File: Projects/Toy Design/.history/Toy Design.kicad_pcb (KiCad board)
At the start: 2 copper layers, 170 x 120 mm, 85 parts, among them J1 Conn_01x01_Pin, J2 Conn_01x01_Pin, J3 FTSH-107-01-X-DV-K-TR, SW1 5GTH935, SW2 5GTH935, U1 TLV61048DBVR, U10 STM32G030K6T6, U11 MCP3208-CI/SL, U12 74HC595, U13 74HC595, U14 74HC595, U15 74HC595, U16 74HC595, U17 74HC595, U2 MCP73123, U3 NCP1117-5.0_SOT223, U4 MLX90333, U5 A1330, U6 A1330, U7 NCP1117-3.3_SOT223, U8 A1330, U9 TXU0104

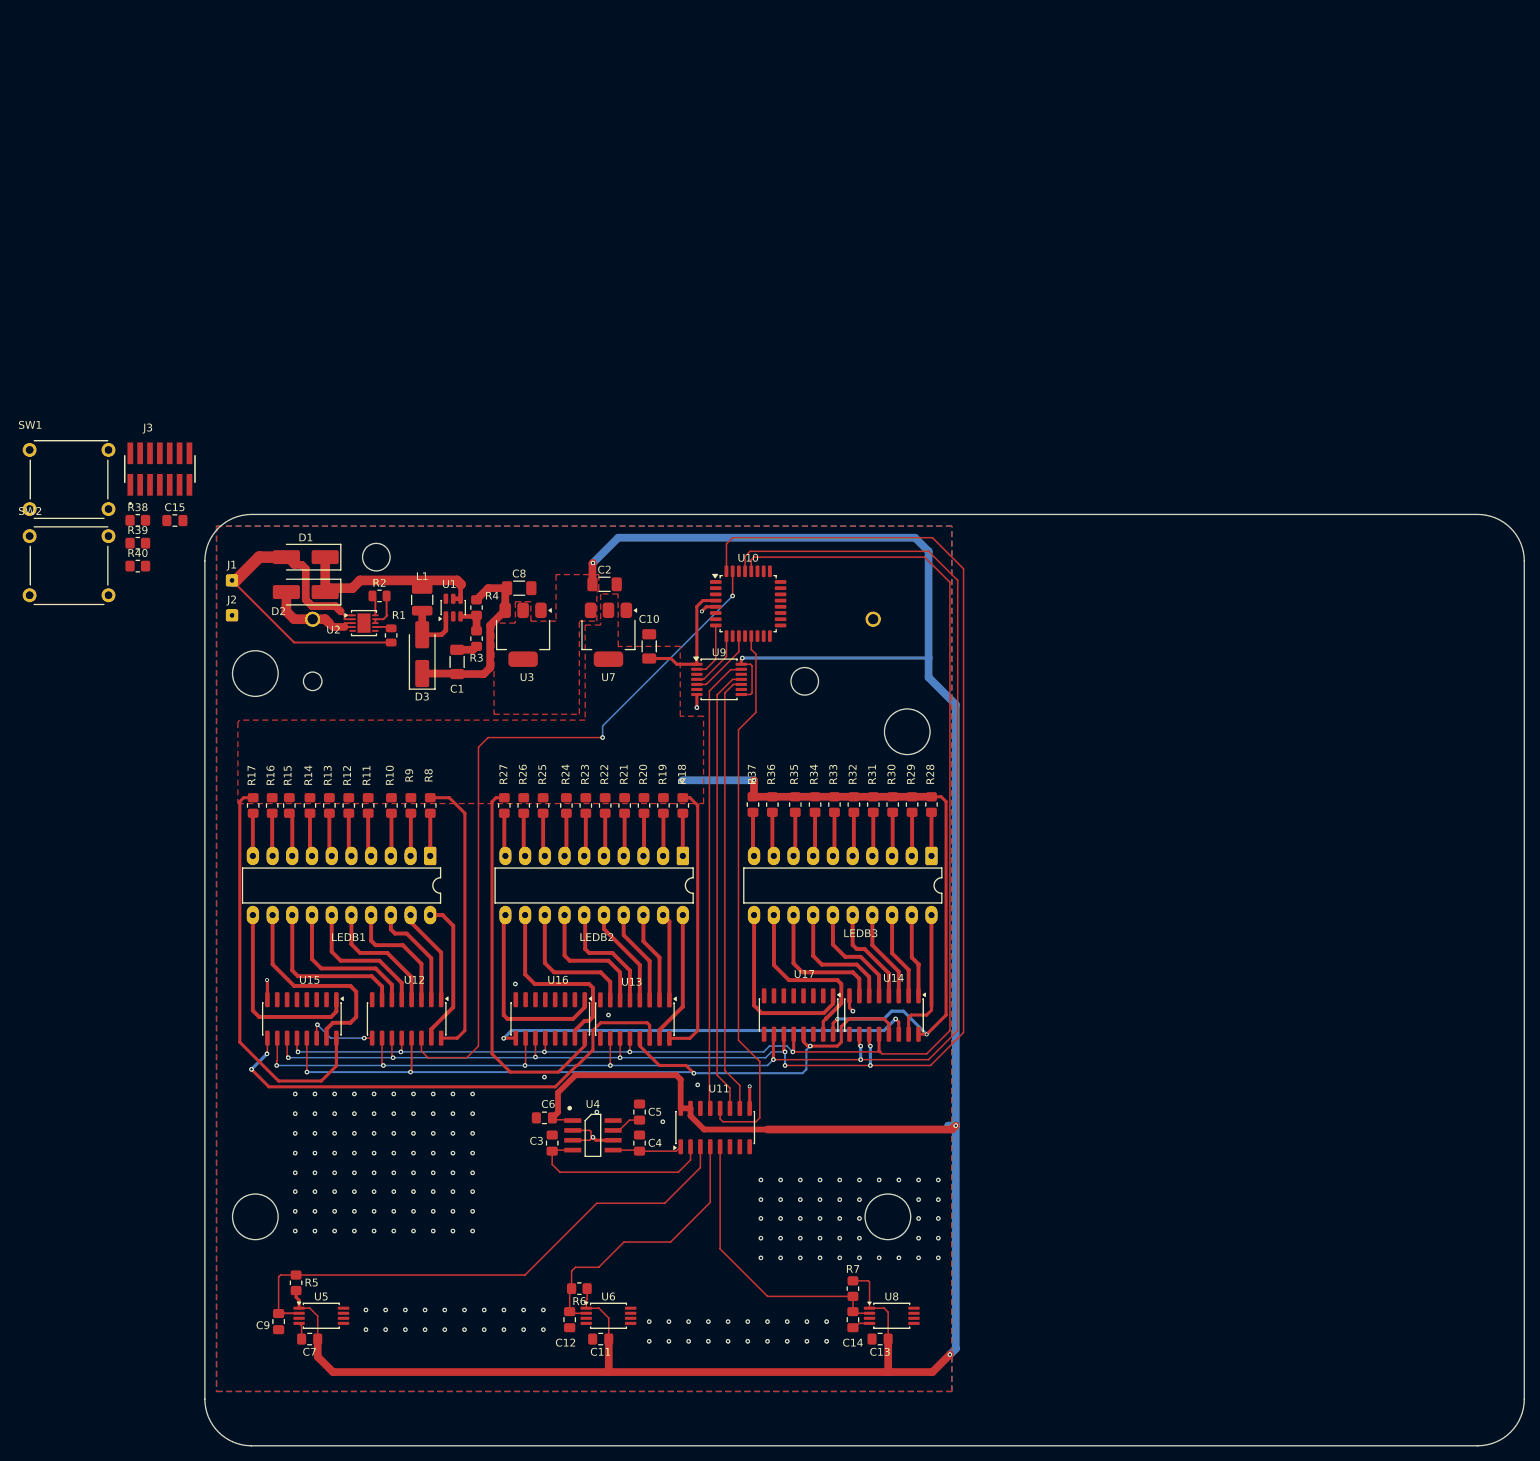
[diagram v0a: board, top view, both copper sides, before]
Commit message: Continued layout on design file with claude
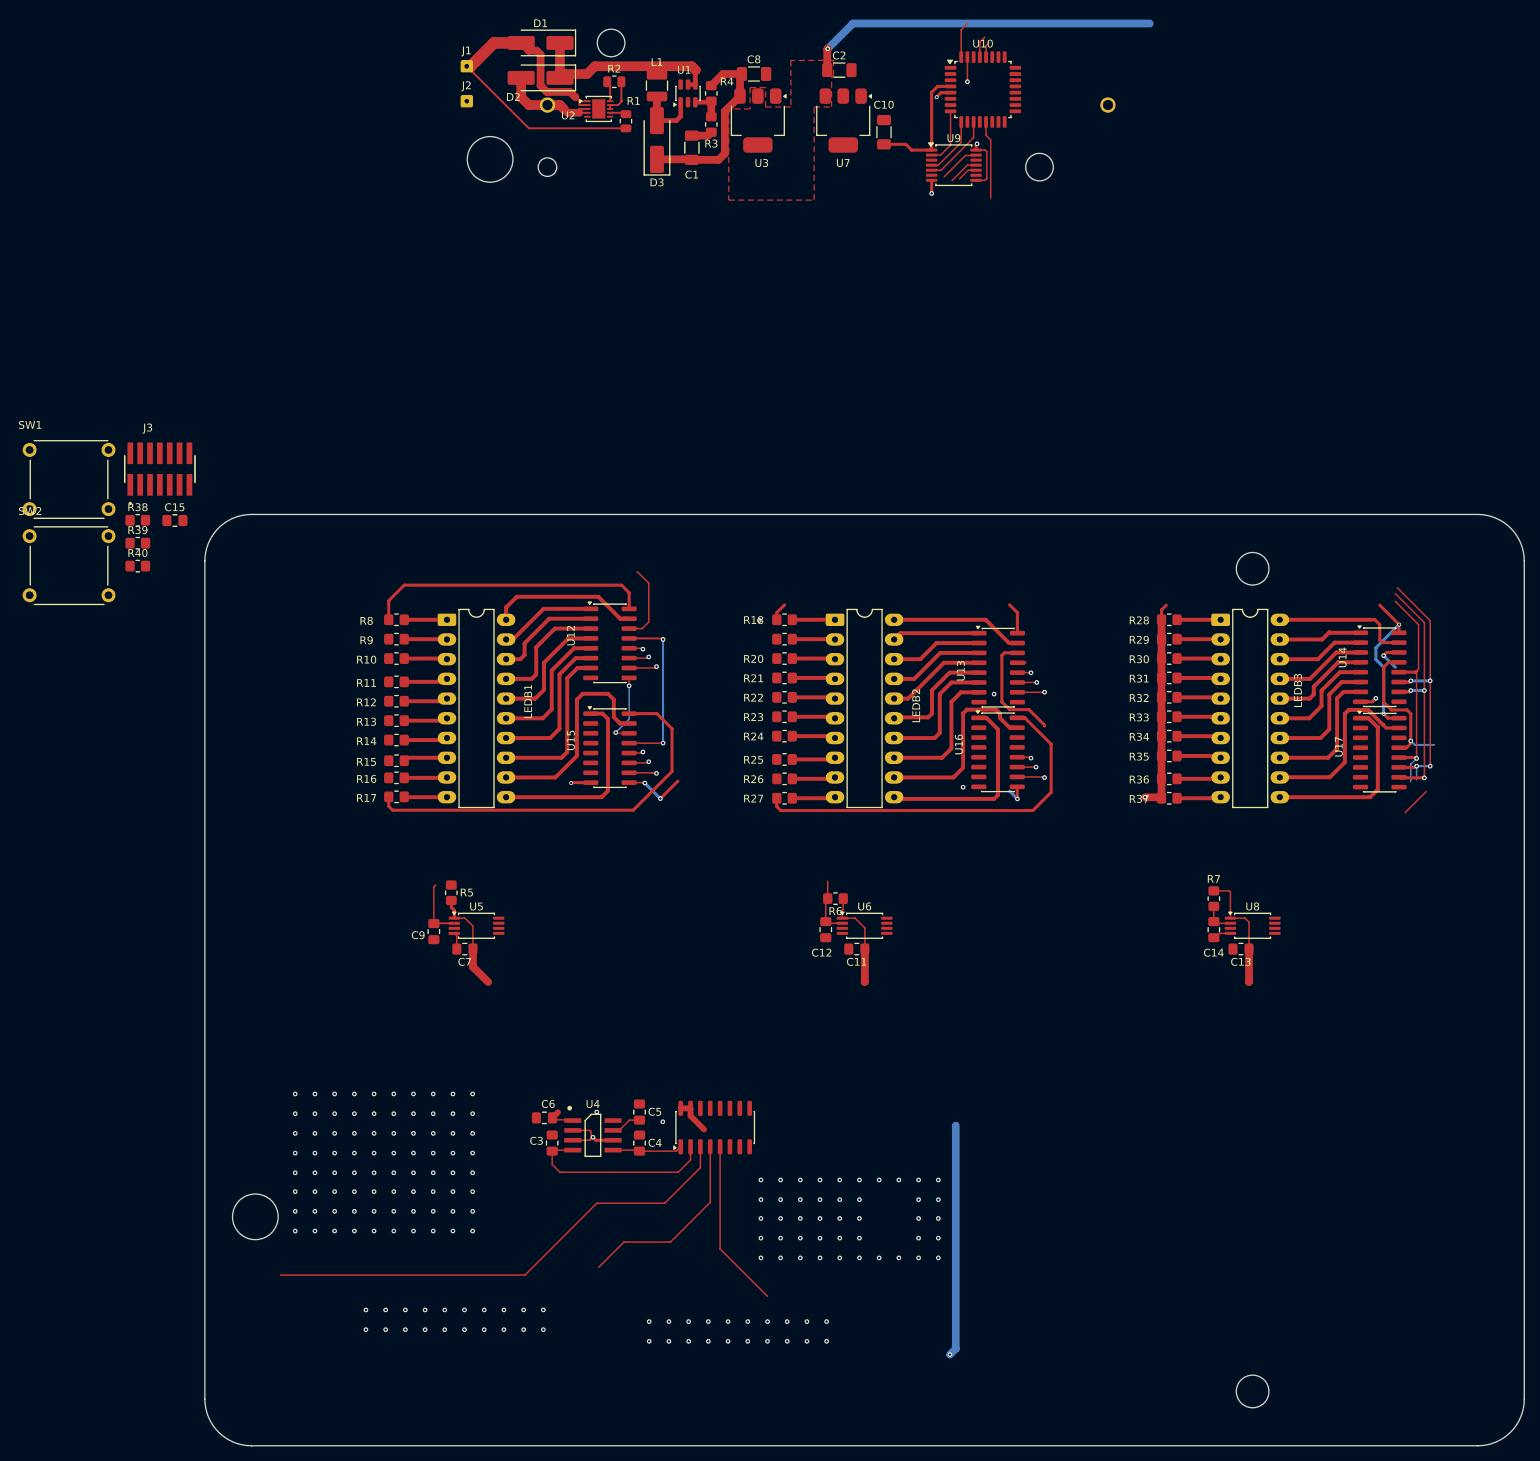
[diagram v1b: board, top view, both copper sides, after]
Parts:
- moved U17 82.2 mm to (247.9, 62.2), turned to 0 degrees
- moved U14 78.0 mm to (247.9, 51.2), turned to 0 degrees
- moved BT1 72.8 mm to (176.8, -21.2)
- moved C1 72.8 mm to (159.2, -15.8)
- moved C10 72.8 mm to (184.0, -17.8)
- moved C2 72.8 mm to (178.2, -25.8)
- moved C8 72.8 mm to (167.2, -25.2)
- moved D1 72.8 mm to (139.8, -29.2)
- moved D2 72.8 mm to (139.8, -24.8)
- moved D3 72.8 mm to (154.8, -16.8)
- moved J1 72.8 mm to (130.2, -26.2)
- moved J2 72.8 mm to (130.2, -21.8)
- moved L1 72.8 mm to (154.8, -23.8)
- moved R1 72.8 mm to (150.8, -19.2)
- moved R2 72.8 mm to (149.2, -24.2)
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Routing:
- net +5V: track 372.7 -> 133.5 mm, vias 4 -> 3
- net SPI2_SCK_LED: track 203.3 -> 49.6 mm
- net ~{SRCLR}: track 199.6 -> 49.0 mm
- net RCLK_LED: track 184.2 -> 38.8 mm
- net SPI2_MOSI_LED: track 93.4 -> 13.2 mm, vias 2 -> 1
- net +3.3V: track 274.3 -> 208.5 mm
- net ~{OE}: track 102.6 -> 42.9 mm, vias 4 -> 3
- net MISO_SPI1: track 71.2 -> 14.0 mm
- net Net-(U11-~{CS}/SHDN): track 56.9 -> 2.57 mm
- net Net-(U11-Din): track 57.9 -> 3.94 mm
- net Net-(U11-CLK): track 59.1 -> 5.27 mm
- net Net-(U14-SER): track 55.2 -> 7.24 mm
- net Net-(U13-SER): track 63.8 -> 23.0 mm
- net OUT_U8: track 37.0 -> 26.0 mm
- net OUT_U6: track 36.2 -> 32.5 mm
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- removed copper zone on F.Cu, net +3.3V
- removed copper zone on B.Cu, net GND
- removed copper zone on F.Cu, net GND
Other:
- board size 170 x 120 mm -> 170 x 168.7 mm

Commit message: final update from desktop
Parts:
- moved SW2 204.6 mm to (255.5, 141.5)
- moved BT1 126.9 mm to (146.5, 102.0)
- moved C1 126.9 mm to (129.0, 107.5)
- moved C10 126.9 mm to (153.8, 105.5)
- moved C2 126.9 mm to (148.0, 97.5)
- moved C8 126.9 mm to (137.0, 98.0)
- moved D1 126.9 mm to (109.5, 94.0)
- moved D2 126.9 mm to (109.5, 98.5)
- moved D3 126.9 mm to (124.5, 106.5)
- moved J1 126.9 mm to (100.0, 97.0)
- moved J2 126.9 mm to (100.0, 101.5)
- moved L1 126.9 mm to (124.5, 99.5)
- moved R1 126.9 mm to (120.5, 104.1)
- moved R2 126.9 mm to (119.0, 99.0)
- moved R3 126.9 mm to (131.5, 104.5)
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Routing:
- net OUT_U5: track 70.2 -> 10.4 mm
- net +5V: track 133.5 -> 103.6 mm, vias 3 -> 4
- net OUT_U6: track 32.5 -> 7.54 mm
- net OUT_U8: track 26.0 -> 4.19 mm
- net +3.3V: track 208.5 -> 210.5 mm
- net Net-(U12-QA): track 19.2 -> 17.7 mm
- net GND: vias 173 -> 171
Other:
- board size 170 x 168.7 mm -> 170 x 120 mm

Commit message: small updates
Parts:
- J3: moved to B.Cu
- moved R38 127.2 mm to (198.5, 95.0), turned to 180 degrees
- moved C15 124.3 mm to (198.5, 97.5)
- moved J3 123.6 mm to (191.2, 97.5), turned to 90 degrees
- moved R39 111.2 mm to (175.0, 104.2), turned to 180 degrees
- moved R40 107.5 mm to (170.2, 107.2), turned to 180 degrees
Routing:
- net +5V: track 103.6 -> 161.5 mm, vias 4 -> 6
- net Net-(U10-PB1): track 0.00 -> 4.73 mm
- net Net-(U10-PB0): track 0.00 -> 3.39 mm
- net NRST: track 0.00 -> 2.52 mm

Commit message: updates
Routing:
- net ~{OE}: track 42.9 -> 115.0 mm, vias 3 -> 4
- net SPI2_MOSI_LED: track 13.2 -> 48.4 mm
- net ~{SRCLR}: track 49.0 -> 62.8 mm
- net SPI2_SCK_LED: track 49.6 -> 63.1 mm
- net RCLK_LED: track 38.8 -> 52.0 mm
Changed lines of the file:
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@@
+	)
+	(segment
+		(start 152.94 62.11)
+		(end 152.94 48.86)
+		(width 0.2)
+		(layer "B.Cu")
+		(net "RCLK_LED")
 	)
 	(segment
@@
 	)
 	(segment
+		(start 154.69 51.11)
+		(end 154.69 64.86)
+		(width 0.2)
+		(layer "B.Cu")
+		(net "~{SRCLR}")
+	)
+	(segment
 		(start 251.88 54.19)
 		(end 253.63 54.19)
@@
 	)
 	(segment
-		(start 152.19 38.86)
-		(end 153.69 40.36)
+		(start 151.165 46.205)
+		(end 154.983529 46.205)
 		(width 0.2)
 		(layer "F.Cu")
@@
 	)
 	(segment
-		(start 153.69 45.36)
-		(end 152.845 46.205)
-		(width 0.2)
-		(layer "F.Cu")
-		(net "SPI2_MOSI_LED")
-	)
-	(segment
-		(start 152.845 46.205)
-		(end 151.165 46.205)
-		(width 0.2)
-		(layer "F.Cu")
-		(net "SPI2_MOSI_LED")
-	)
-	(segment
-		(start 153.69 40.36)
-		(end 153.69 45.36)
+		(start 164.25 55.471471)
+		(end 164.25 83.75)
 		(width 0.2)
 		(layer "F.Cu")
@@
 		(net "SPI2_MOSI_LED")
 	)
+	(segment
+		(start 154.983529 46.205)
+		(end 164.25 55.471471)
+		(width 0.2)
+		(layer "F.Cu")
+		(net "SPI2_MOSI_LED")
+	)
 	(via
 		(at 164.5 99)
@@
 		(end 254.38 63.94)
 		(width 0.254)
+		(layer "B.Cu")
+		(net "SPI2_SCK_LED")
+	)
+	(segment
+		(start 153.69 49.86)
+		(end 153.69 63.36)
+		(width 0.2)
 		(layer "B.Cu")
 		(net "SPI2_SCK_LED")
@@
 	)
 	(segment
+		(start 202.164999 50.61)
+		(end 204.25 48.524999)
+		(width 0.4)
+		(layer "F.Cu")
+		(net "~{OE}")
+	)
+	(segment
 		(start 249.015 50.555)
 		(end 248.38 51.19)
@@
 	)
 	(segment
+		(start 204.25 48.524999)
+		(end 204.25 37.75)
+		(width 0.4)
+		(layer "F.Cu")
+		(net "~{OE}")
+	)
+	(segment
+		(start 203.5 37)
+		(end 202.75 37)
+		(width 0.4)
+		(layer "F.Cu")
+		(net "~{OE}")
+	)
+	(segment
 		(start 251.329999 61.555)
 		(end 250.355 61.555)
@@
 	)
 	(segment
+		(start 204.25 37.75)
+		(end 203.5 37)
+		(width 0.4)
+		(layer "F.Cu")
+		(net "~{OE}")
+	)
+	(segment
 		(start 248.38 51.19)
 		(end 248.38 55.69)
@@
 	)
 	(via
+		(at 202.75 37)
+		(size 0.6)
+		(drill 0.3)
+		(layers "F.Cu" "B.Cu")
+		(net "~{OE}")
+	)
+	(via
 		(at 155.54 60.96)
 		(size 0.6)
 		(drill 0.3)
 		(layers "F.Cu" "B.Cu")
+		(net "~{OE}")
+	)
+	(segment
+		(start 157.75 37)
+		(end 202.75 37)
+		(width 0.254)
+		(layer "B.Cu")
+		(net "~{OE}")
+	)
+	(segment
+		(start 155.54 47.61)
+		(end 155.5 47.57)
+		(width 0.254)
+		(layer "B.Cu")
 		(net "~{OE}")
 	)
@@
 	)
 	(segment
+		(start 155.5 47.57)
+		(end 155.5 39.25)
+		(width 0.254)
+		(layer "B.Cu")
+		(net "~{OE}")
+	)
+	(segment
 		(start 155.54 47.61)
 		(end 155.54 60.96)
 		(width 0.254)
 		(layer "B.Cu")
+		(net "~{OE}")
+	)
+	(segment
+		(start 155.5 39.25)
+		(end 157.75 37)
+		(width 0.254)
+		(layer "B.Cu")

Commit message: Cleaned up some traces
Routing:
- net OUT_U5: track 10.4 -> 179.9 mm
- net OUT_U6: track 7.54 -> 89.5 mm
- net OUT_U8: track 4.19 -> 64.0 mm
- net Net-(U10-PB1): track 4.73 -> 56.8 mm
- net NRST: track 2.52 -> 53.6 mm, vias 0 -> 2
- net SWDIO: track 0.00 -> 34.6 mm, vias 0 -> 1
- net SWCLK: track 0.00 -> 31.6 mm, vias 0 -> 1
- net MISO_SPI1: track 14.0 -> 42.5 mm
- net +3.3V: track 210.5 -> 238.0 mm
- net +5V: track 161.5 -> 158.0 mm
- net RCLK_LED: track 52.0 -> 48.7 mm
- net ~{OE}: track 115.0 -> 111.8 mm
- net GND: track 29.2 -> 31.6 mm
- net SPI2_SCK_LED: track 63.1 -> 61.3 mm
